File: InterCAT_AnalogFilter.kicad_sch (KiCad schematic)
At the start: 21 parts, among them T1 LM-NP-1001-B1L, T4 LM-NP-1001-B1L, U4 MCP6002, U6 MCP6002

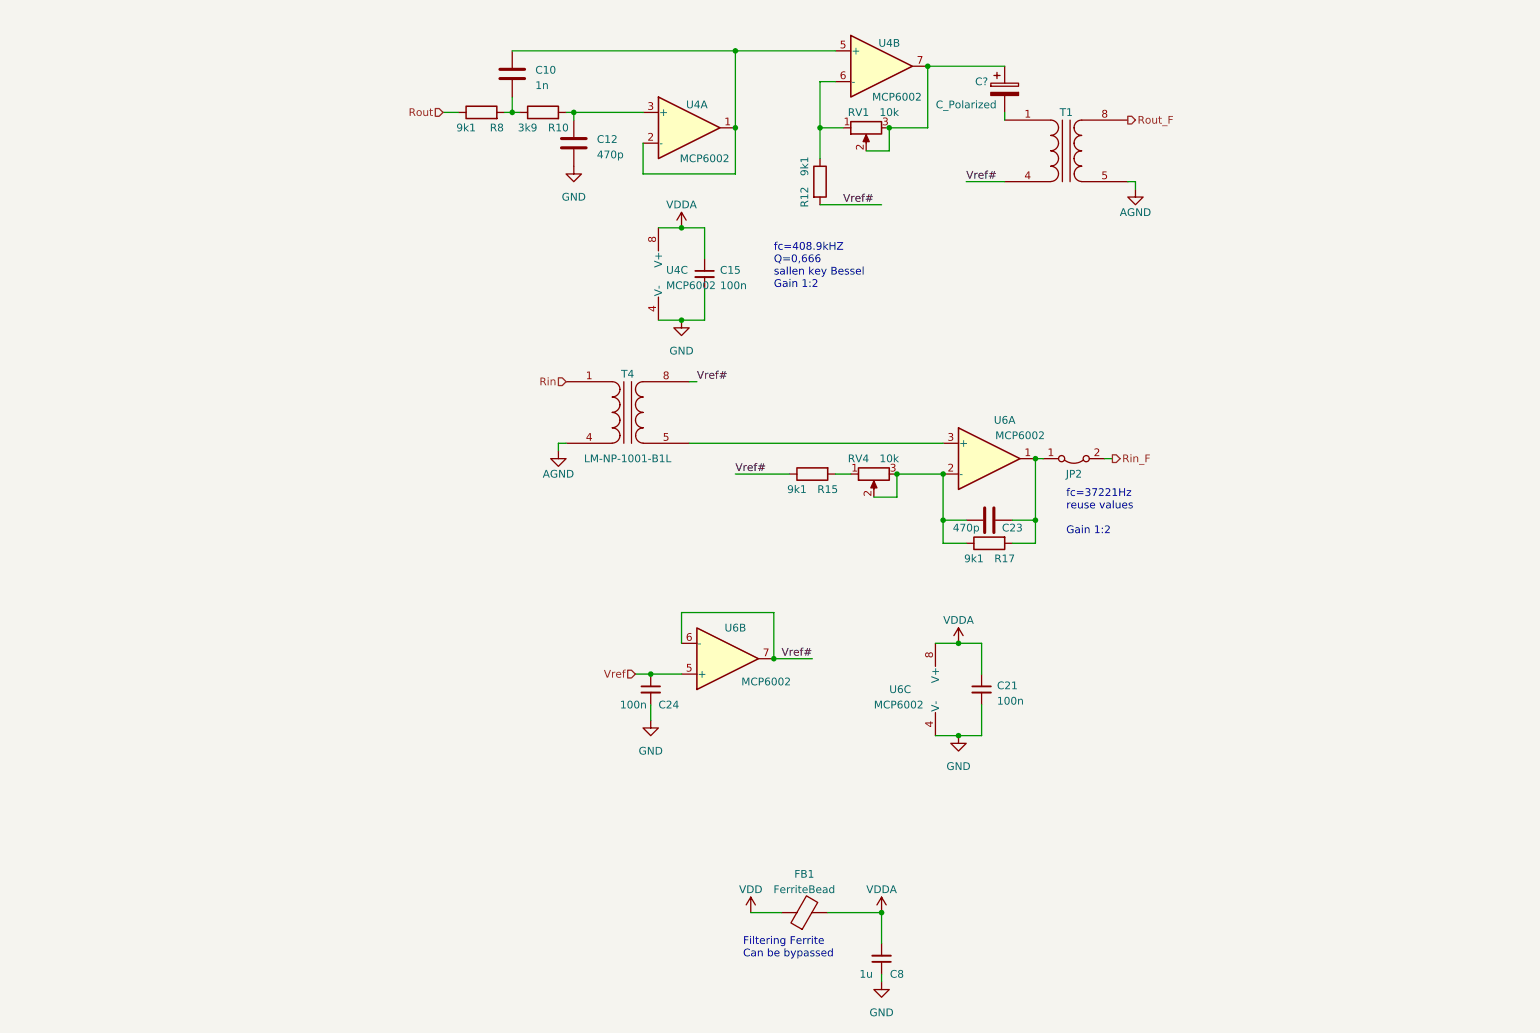
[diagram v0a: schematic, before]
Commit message: removed missed cap,reviewed layout
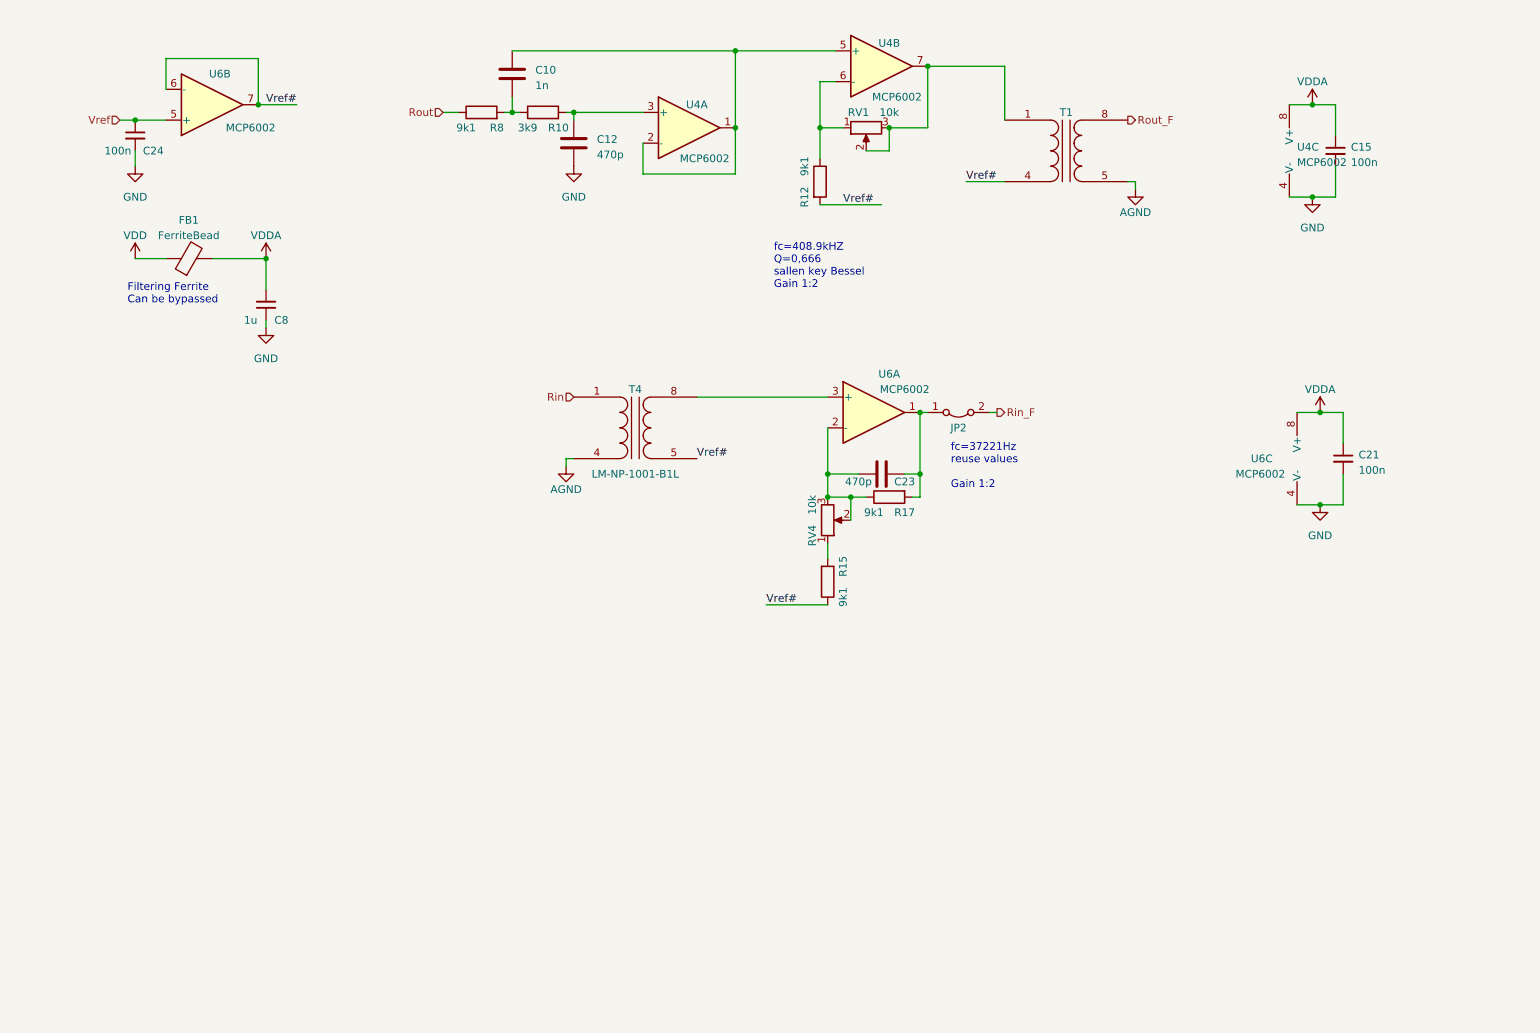
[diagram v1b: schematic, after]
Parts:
- removed C?: C_Polarized, Capacitor_THT:CP_Radial_D5.0mm_P2.50mm, symbol Device:C_Polarized
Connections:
- net Vref#: now also T4.5 (SA); no longer T4.8 (SB)
- net at T1.1 (AA): now also RV1.2, RV1.3, U4.7
- net at U6.3 (+): now also T4.8 (SB); no longer T4.5 (SA)
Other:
- moved on the sheet: C15, C21, C23, C24, C8, FB1, JP2, R15, R17, RV4, T4, U4C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

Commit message: corrected gain of the amplifiers and dyn range, continued PCB
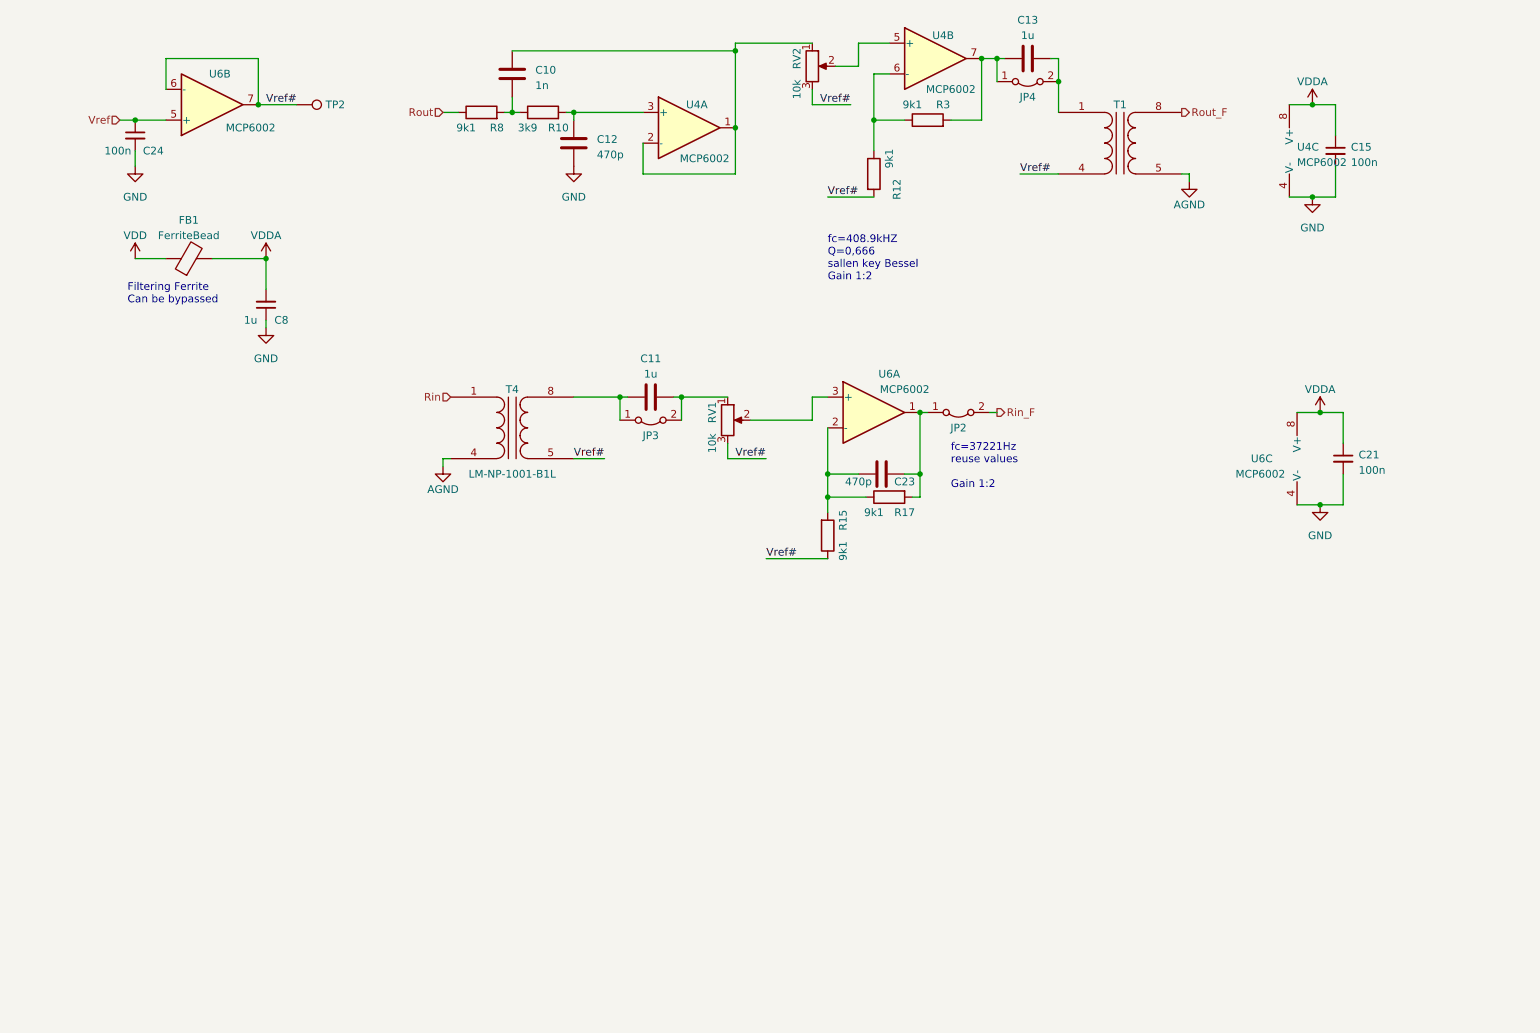
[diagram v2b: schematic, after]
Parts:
- removed RV4: 10k, Potentiometer_THT:Potentiometer_Bourns_3386P_Vertical, symbol Device:R_Potentiometer
- added C11, C13: 1u, Capacitor_SMD:C_0805_2012Metric, symbol Device:C
- added JP3, JP4: Jumper_2_Bridged, Jumper:SolderJumper-2_P1.3mm_Bridged_RoundedPad1.0x1.5mm, symbol Jumper:Jumper_2_Bridged
- added R3: 9k1, Resistor_SMD:R_0603_1608Metric, symbol Device:R
- added RV2: 10k, Potentiometer_THT:Potentiometer_Bourns_3386P_Vertical, symbol Device:R_Potentiometer
- added TP2: TestPoint, TestPoint:TestPoint_Pad_D1.5mm, symbol Connector:TestPoint
- C10: LCSC C28323 -> (none)
- C8: Note X7R -> 50V X7R
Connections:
- net Vref#: now also RV1.3, RV2.3, TP2.1
- net at R15.2: now also C23.1, R17.1, U6.2 (-)
- net at C10.1, U4.1, U4.2 (-): now also RV2.1; no longer U4.5 (+)
- net at R12.1, U4.6 (-): now also R3.1; no longer RV1.1
- net at U6.3 (+): now also RV1.2; no longer T4.8 (SB)
- new net: C11.2, JP3.2 (B), RV1.1
- new net: C13.1, JP4.1 (A), R3.2, U4.7
- new net: C13.2, JP4.2 (B), T1.1 (AA)
- new net: RV2.2, U4.5 (+)
- new net: C11.1, JP3.1 (A), T4.8 (SB)
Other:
- moved on the sheet: R12, R15, T1, T4, U4B

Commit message: Started Version 2.0, migrated to STM32, changed some symbols, added 3V3 Supply
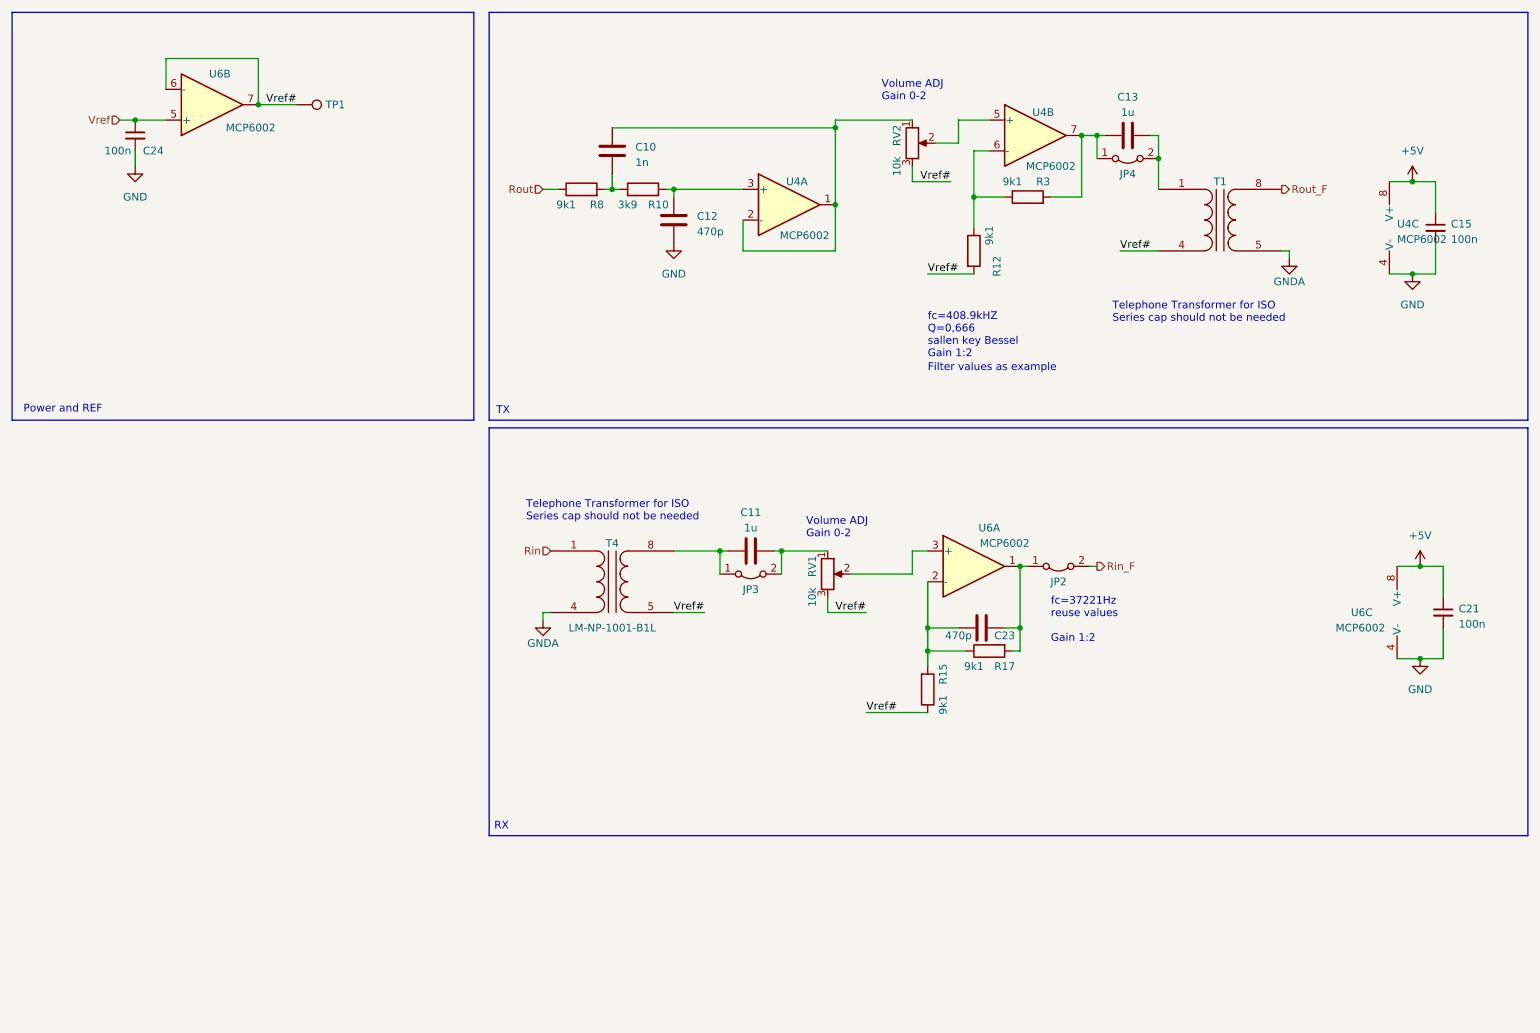
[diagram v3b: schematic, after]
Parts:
- removed C8: 1u, Capacitor_SMD:C_0805_2012Metric, symbol Device:C_Small
- removed FB1: FerriteBead, Resistor_SMD:R_0603_1608Metric, symbol Device:FerriteBead
- renumbered TP2 to TP1
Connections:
- net VDDA renamed +5V
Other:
- note added: "Filter values as example"
- note added: "Power and REF"
- note added: "RX"
- note added: "TX"
- note added: "Telephone Transformer for ISO Series cap should not be needed"
- note added: "Volume ADJ Gain 0-2"
- note removed: "Filtering Ferrite Can be bypassed"
- moved on the sheet: C10, C11, C12, C13, C15, C21, C23, JP2, JP3, JP4, R10, R12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

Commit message: added trafo bypass, added zener reg, added todo
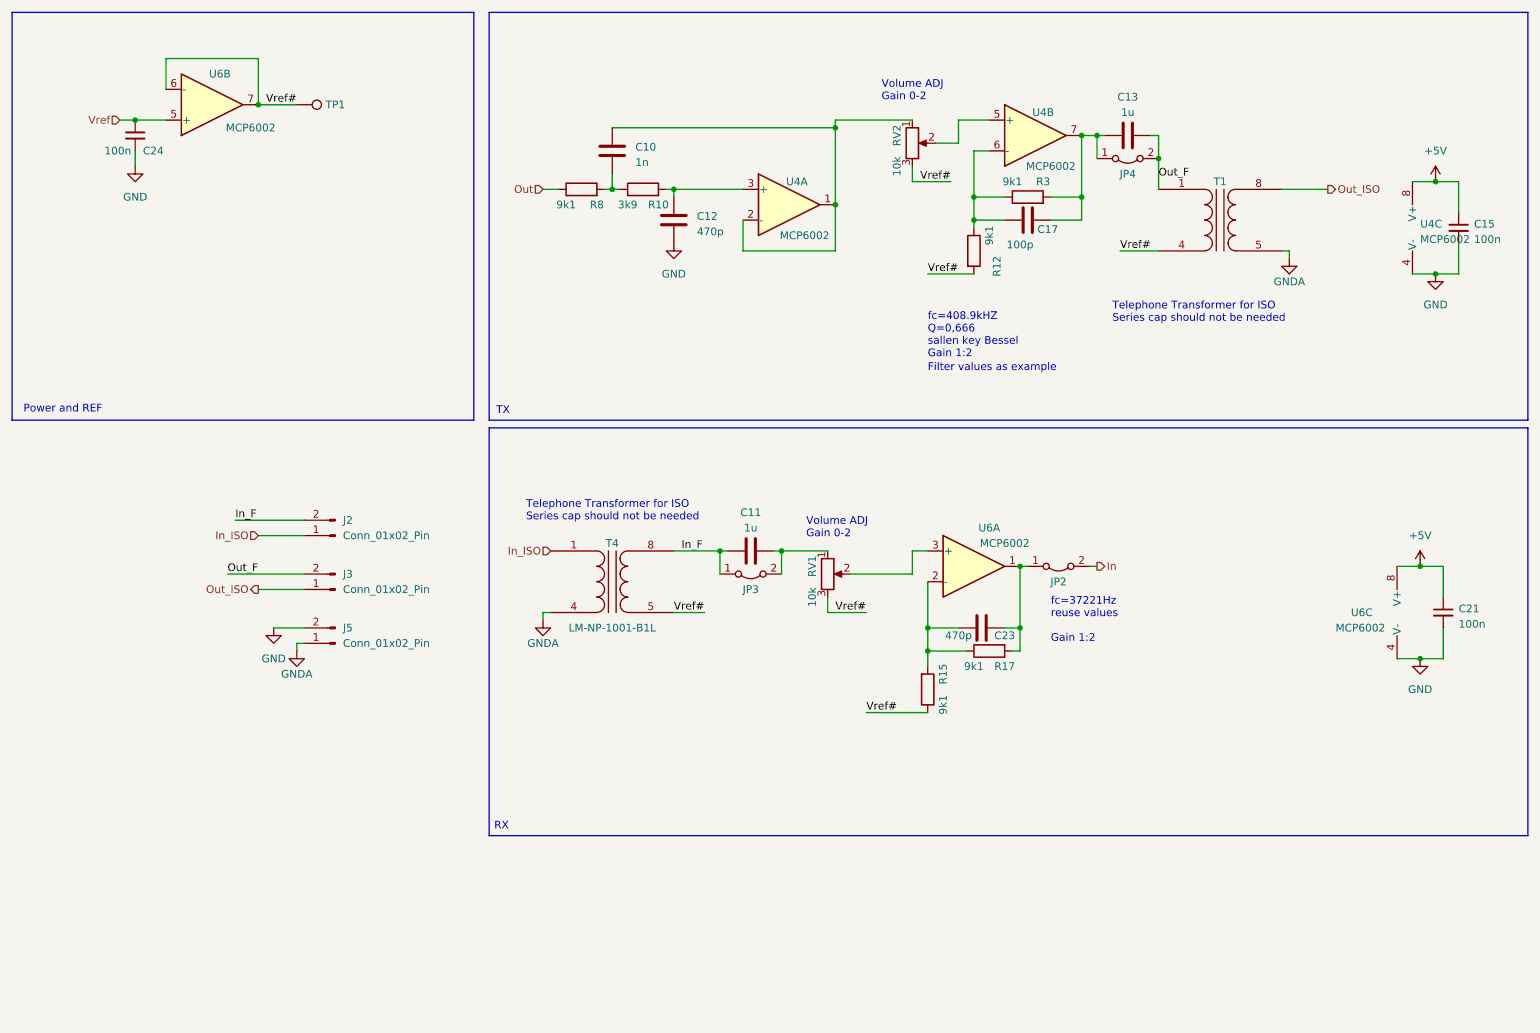
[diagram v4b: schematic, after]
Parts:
- added C17: 100p, Capacitor_SMD:C_0603_1608Metric, symbol Device:C
- added J2, J3, J5: Conn_01x02_Pin, Connector_PinHeader_2.54mm:PinHeader_1x02_P2.54mm_Vertical, symbol Connector:Conn_01x02_Pin
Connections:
- net GND: now also J5.2 (Pin_2)
- net GNDA: now also J5.1 (Pin_1)
- net at R12.1, R3.1, U4.6 (-): now also C17.1
- net at C13.1, JP4.1 (A), R3.2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: now also C17.2
- net Out_F: now reaches C13.2, JP4.2 (B), T1.1 (AA)
- net Out_F: now also J3.2 (Pin_2)
- net In_F: now reaches C11.1, JP3.1 (A), T4.8 (SB)
- net In_F: now also J2.2 (Pin_2)
- net Rin renamed In_ISO
- net In_ISO: now also J2.1 (Pin_1)
- net Rin_F renamed In
- net Rout renamed Out
- net Rout_F renamed Out_ISO
- net Out_ISO: now also J3.1 (Pin_1)
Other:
- moved on the sheet: C15, U4C

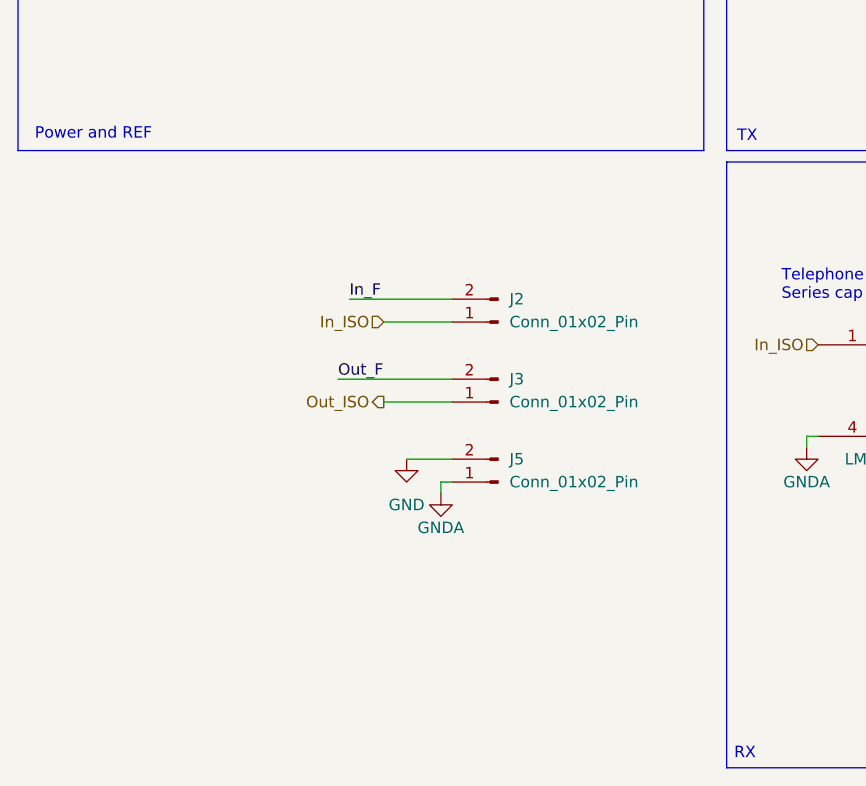
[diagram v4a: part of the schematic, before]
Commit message: added iso bypass, removed RS232, added Extra opto and prog connector
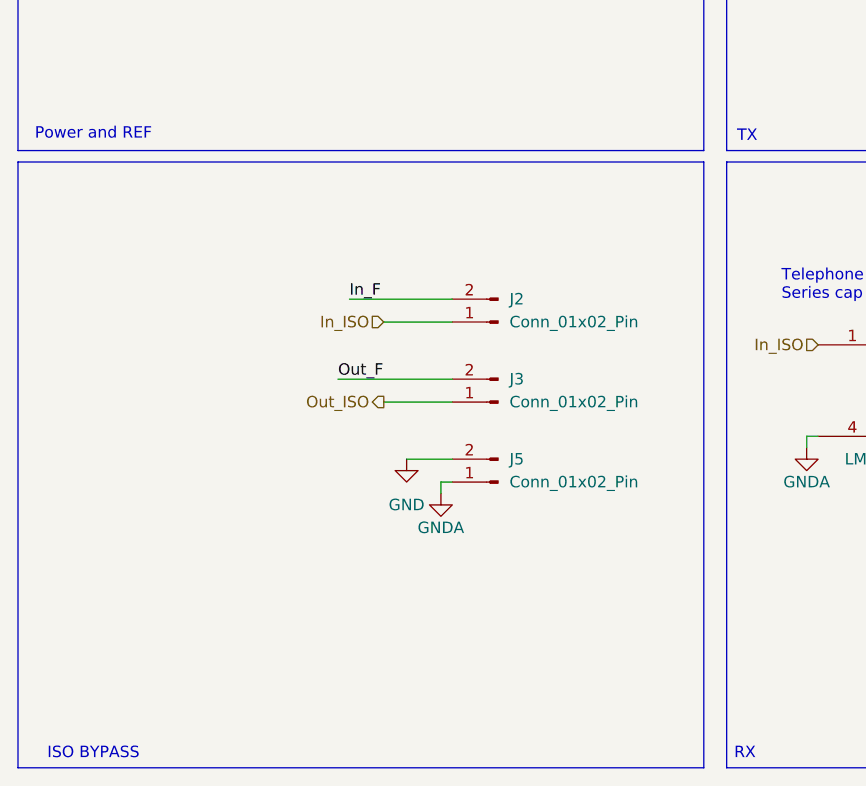
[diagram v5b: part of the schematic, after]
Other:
- note added: "ISO BYPASS"
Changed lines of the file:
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@@
+		)
+	)
+	(rectangle
+		(start 25.4 95.25)
+		(end 101.6 162.56)
+		(stroke
+			(width 0)
+			(type default)
+		)
+		(fill
+			(type none)
 		)
 	)
@@
 		)
 	)
+	(text "ISO BYPASS"
+		(exclude_from_sim no)
+		(at 33.782 161.036 0)
+		(effects
+			(font
+				(size 1.27 1.27)
+			)
+		)
+	)
